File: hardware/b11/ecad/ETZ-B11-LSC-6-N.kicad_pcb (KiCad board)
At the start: 2 copper layers, 112.3 x 85.8 mm, 0 parts

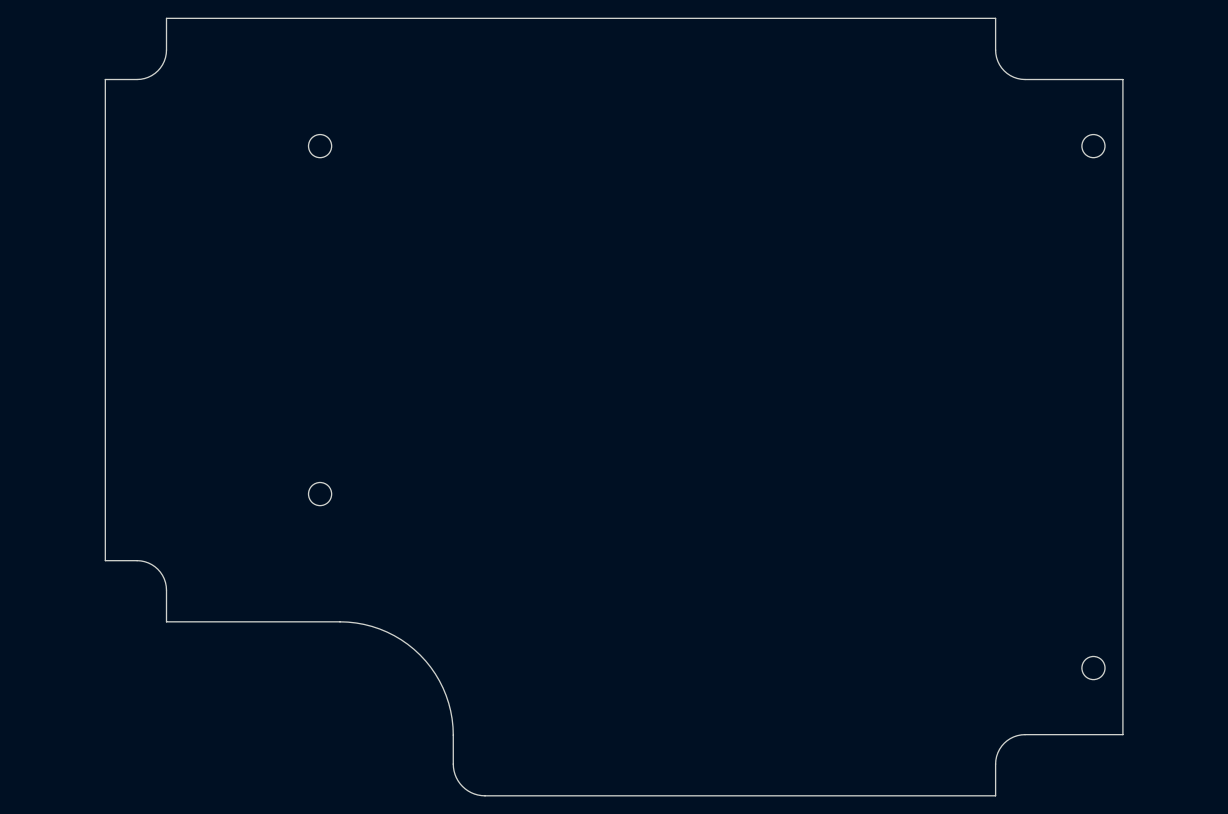
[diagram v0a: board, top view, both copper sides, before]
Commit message: feat(hardware/b11): place MX hotswap switches on normal-profile carrier PCBs
Add place-b11-switches.py with SWIG pre-init workaround (plug must be
created and FootprintLoad called before LoadBoard or SWIG type registry
gets corrupted). Layout: 5-col boards get 18 switches (15 main + 3
thumb at cols 2-4), 6-col get 22 (18 main + 4 thumb at cols 2-5).

Also refresh all 20 PCB outline DXFs from latest MCAD release and add
MX_V2 footprint library as a submodule.

Co-Authored-By: Claude Sonnet 4.6 <noreply@anthropic.com>
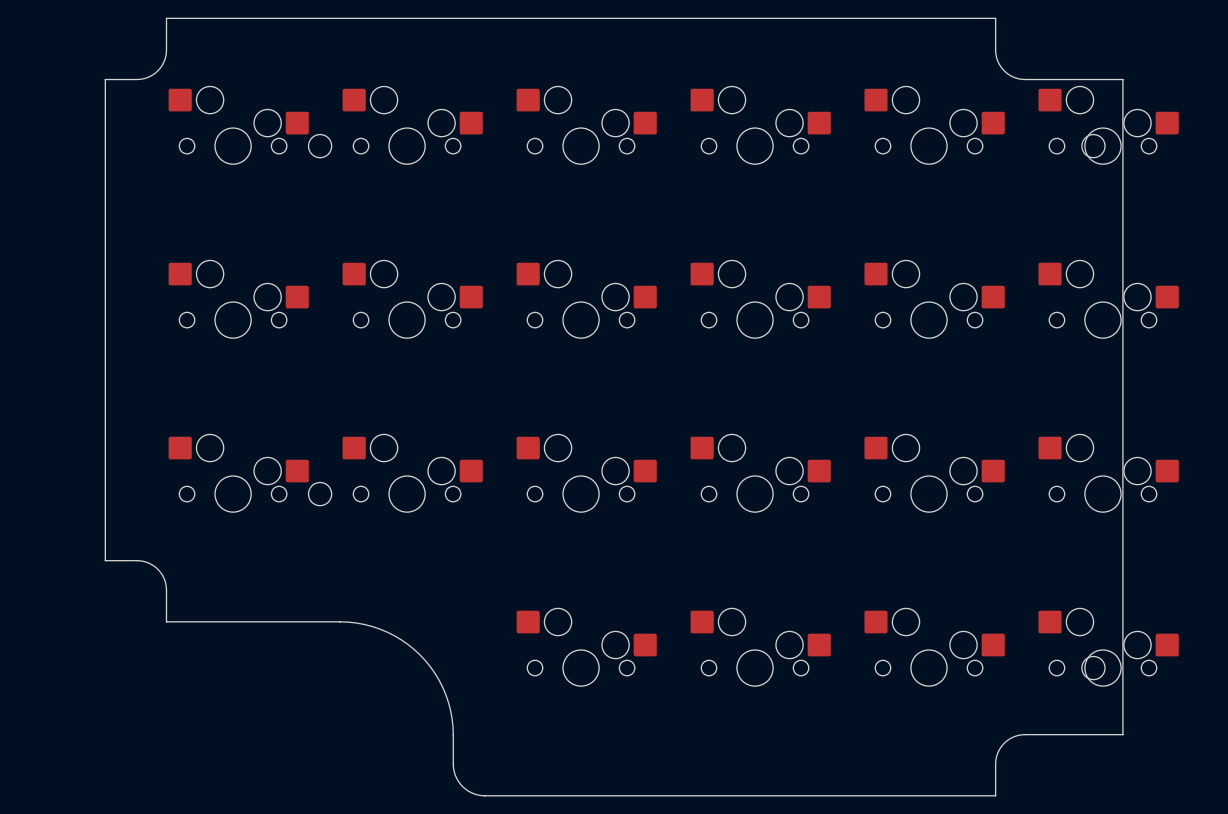
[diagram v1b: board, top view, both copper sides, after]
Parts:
- added SW1: MX-Hotswap-1U, MX-Hotswap-1U, F.Cu at (106.4, 73.3)
- added SW10: MX-Hotswap-1U, MX-Hotswap-1U, F.Cu at (164.0, 92.5)
- added SW11: MX-Hotswap-1U, MX-Hotswap-1U, F.Cu at (183.2, 92.5)
- added SW12: MX-Hotswap-1U, MX-Hotswap-1U, F.Cu at (202.4, 92.5)
- added SW13: MX-Hotswap-1U, MX-Hotswap-1U, F.Cu at (106.4, 111.7)
- added SW14: MX-Hotswap-1U, MX-Hotswap-1U, F.Cu at (125.6, 111.7)
- added SW15: MX-Hotswap-1U, MX-Hotswap-1U, F.Cu at (144.8, 111.7)
- added SW16: MX-Hotswap-1U, MX-Hotswap-1U, F.Cu at (164.0, 111.7)
- added SW17: MX-Hotswap-1U, MX-Hotswap-1U, F.Cu at (183.2, 111.7)
- added SW18: MX-Hotswap-1U, MX-Hotswap-1U, F.Cu at (202.4, 111.7)
- added SW19: MX-Hotswap-1U, MX-Hotswap-1U, F.Cu at (144.8, 130.9)
- added SW2: MX-Hotswap-1U, MX-Hotswap-1U, F.Cu at (125.6, 73.3)
- added SW20: MX-Hotswap-1U, MX-Hotswap-1U, F.Cu at (164.0, 130.9)
- added SW21: MX-Hotswap-1U, MX-Hotswap-1U, F.Cu at (183.2, 130.9)
- added SW22: MX-Hotswap-1U, MX-Hotswap-1U, F.Cu at (202.4, 130.9)
- added SW3: MX-Hotswap-1U, MX-Hotswap-1U, F.Cu at (144.8, 73.3)
- added SW4: MX-Hotswap-1U, MX-Hotswap-1U, F.Cu at (164.0, 73.3)
- added SW5: MX-Hotswap-1U, MX-Hotswap-1U, F.Cu at (183.2, 73.3)
- added SW6: MX-Hotswap-1U, MX-Hotswap-1U, F.Cu at (202.4, 73.3)
- added SW7: MX-Hotswap-1U, MX-Hotswap-1U, F.Cu at (106.4, 92.5)
- added SW8: MX-Hotswap-1U, MX-Hotswap-1U, F.Cu at (125.6, 92.5)
- added SW9: MX-Hotswap-1U, MX-Hotswap-1U, F.Cu at (144.8, 92.5)

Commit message: fix(hardware/b11): correct 6-col PCB outlines and regenerate all boards
Update DXF outlines for all 6-col variants (LSC, RSC, LSP, RSP — both
normal and low profile) exported manually from OnShape with the _6
configuration. Regenerate all 16 KiCad PCBs from the corrected outlines
and re-place MX hotswap switches on the 4 normal-profile carrier boards.

Co-Authored-By: Claude Sonnet 4.6 <noreply@anthropic.com>
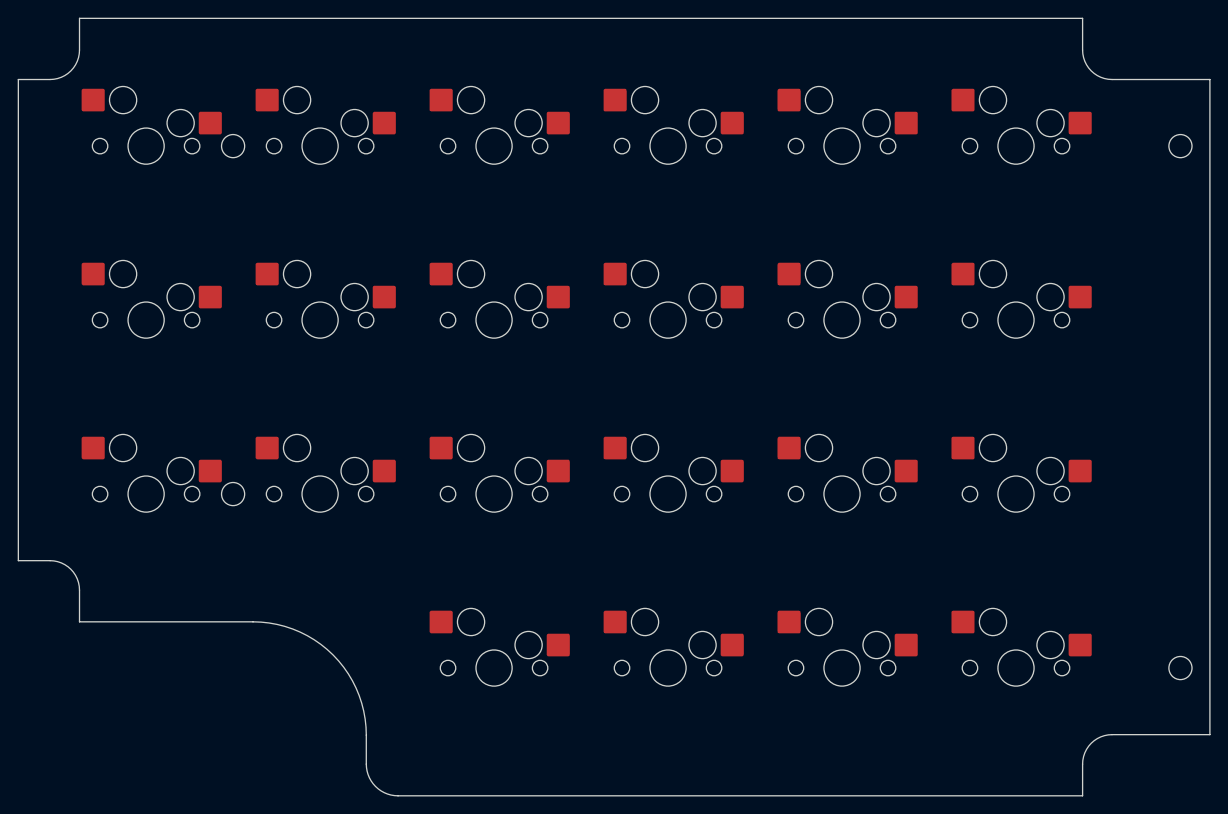
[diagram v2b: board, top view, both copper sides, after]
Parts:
- moved SW11 9.60 mm to (173.6, 92.5)
- moved SW17 9.60 mm to (173.6, 111.7)
- moved SW21 9.60 mm to (173.6, 130.9)
- moved SW5 9.60 mm to (173.6, 73.3)
- moved SW10 9.60 mm to (154.4, 92.5)
- moved SW16 9.60 mm to (154.4, 111.7)
- moved SW20 9.60 mm to (154.4, 130.9)
- moved SW4 9.60 mm to (154.4, 73.3)
- moved SW1 9.60 mm to (96.8, 73.3)
- moved SW13 9.60 mm to (96.8, 111.7)
- moved SW7 9.60 mm to (96.8, 92.5)
- moved SW12 9.60 mm to (192.8, 92.5)
- moved SW14 9.60 mm to (116.0, 111.7)
- moved SW15 9.60 mm to (135.2, 111.7)
- moved SW18 9.60 mm to (192.8, 111.7)
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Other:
- board size 112.3 x 85.8 mm -> 131.5 x 85.8 mm

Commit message: feat(hardware/b11): place hotswap sockets on all carrier boards, south-facing
- Place Kailh MX hotswap sockets (MX-Hotswap-1U) on 4 normal-profile carrier
  boards at 19.2mm pitch, flipped to B.Cu, 180° south-facing orientation
- Place Kailh Choc v1 hotswap sockets (PG1350) on 4 low-profile carrier boards
  at 19.2mm pitch, 180° south-facing orientation
- Add 3D model (Kailh-Choc-Socket-CPG135001S30.step) to PG1350 footprint with
  correct offset/rotation for B.Cu-pad, F.Cu-module placement
- Strip F.SilkS, F.Fab, F.CrtYd top-layer graphics from LP carrier PG1350 footprints
- Rename place-b11-switches.py → place-b11-switches-np.py for symmetry with new lp script
- Add place-b11-switches-lp.py for Choc v1 placement automation

Co-Authored-By: Claude Sonnet 4.6 <noreply@anthropic.com>
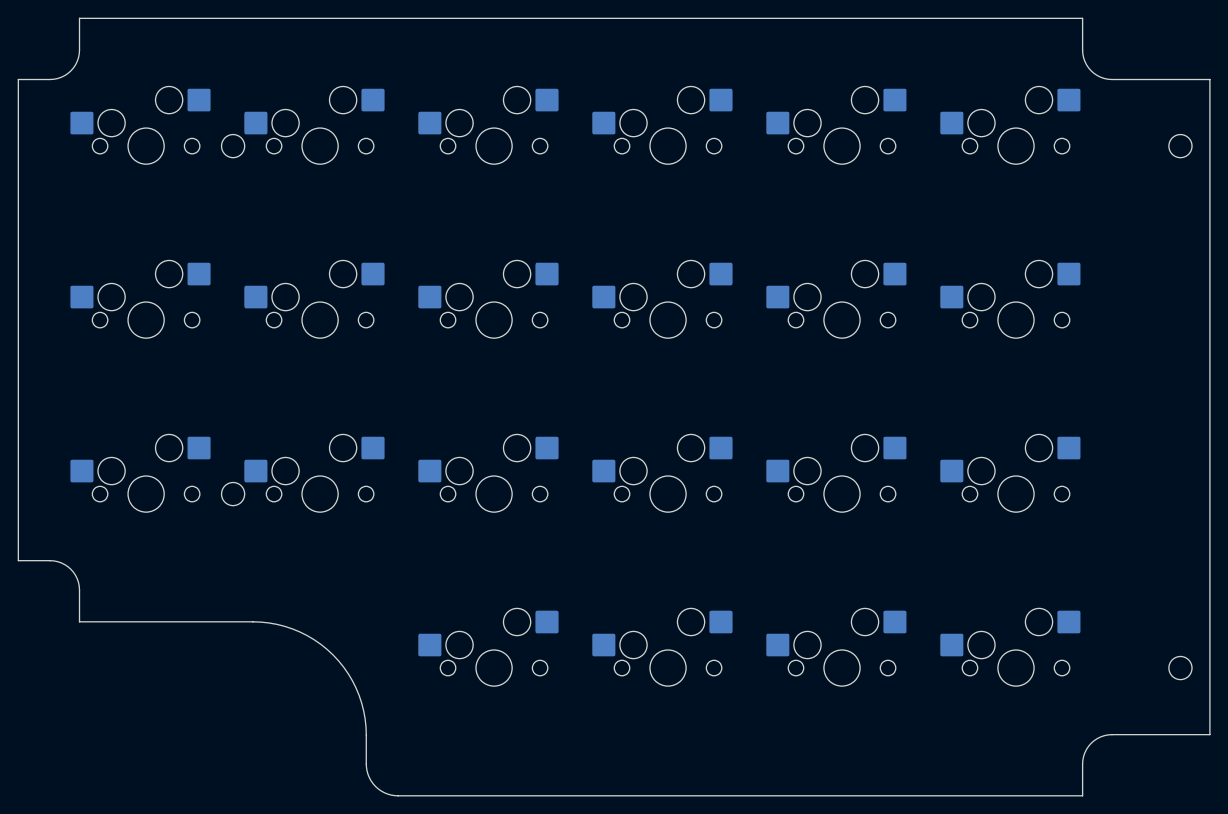
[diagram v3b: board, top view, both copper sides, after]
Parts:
- SW1, SW10, SW11, SW12, SW13, SW14, SW15, SW16, SW17, SW18, SW19, SW2, SW20, SW21, SW22, SW3, SW4, SW5, SW6, SW7, SW8, SW9: moved to B.Cu
- turned SW1 to 180 degrees
- turned SW10 to 180 degrees
- turned SW11 to 180 degrees
- turned SW12 to 180 degrees
- turned SW13 to 180 degrees
- turned SW14 to 180 degrees
- turned SW15 to 180 degrees
- turned SW16 to 180 degrees
- turned SW17 to 180 degrees
- turned SW18 to 180 degrees
- turned SW19 to 180 degrees
- turned SW2 to 180 degrees
- turned SW20 to 180 degrees
- turned SW21 to 180 degrees
- turned SW22 to 180 degrees
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
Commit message: feat(hardware/b11): add SMD 6028 back-mount LED footprint and place on all carrier PCBs
- Add LED_SMD_6028_BackMount footprint with router-safe rounded-rectangle
  slot cutout (3.3 × 3.9 mm, 0.5 mm corners, 1 mm bit), roundrect pads
  (1.4 × 2.8 mm, 25% ratio), silkscreen polarity markers clear of pads
- Add LED_SMD_6028.step 3D model from 3D Content Central
- Add place-b11-leds.py: places 18–22 LEDs per carrier PCB aligned to
  the switch grid, 5.9 mm south of each switch center
- Place LEDs on all 8 carrier PCBs (LSC/RSC × 5/6-col × N/L)

Co-Authored-By: Claude Sonnet 4.6 <noreply@anthropic.com>
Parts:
- added LED1: LED_SMD_6028_BackMount, LED_SMD_6028_BackMount, B.Cu at (96.8, 79.2)
- added LED10: LED_SMD_6028_BackMount, LED_SMD_6028_BackMount, B.Cu at (154.4, 98.4)
- added LED11: LED_SMD_6028_BackMount, LED_SMD_6028_BackMount, B.Cu at (173.6, 98.4)
- added LED12: LED_SMD_6028_BackMount, LED_SMD_6028_BackMount, B.Cu at (192.8, 98.4)
- added LED13: LED_SMD_6028_BackMount, LED_SMD_6028_BackMount, B.Cu at (96.8, 117.6)
- added LED14: LED_SMD_6028_BackMount, LED_SMD_6028_BackMount, B.Cu at (116.0, 117.6)
- added LED15: LED_SMD_6028_BackMount, LED_SMD_6028_BackMount, B.Cu at (135.2, 117.6)
- added LED16: LED_SMD_6028_BackMount, LED_SMD_6028_BackMount, B.Cu at (154.4, 117.6)
- added LED17: LED_SMD_6028_BackMount, LED_SMD_6028_BackMount, B.Cu at (173.6, 117.6)
- added LED18: LED_SMD_6028_BackMount, LED_SMD_6028_BackMount, B.Cu at (192.8, 117.6)
- added LED19: LED_SMD_6028_BackMount, LED_SMD_6028_BackMount, B.Cu at (135.2, 136.8)
- added LED2: LED_SMD_6028_BackMount, LED_SMD_6028_BackMount, B.Cu at (116.0, 79.2)
- added LED20: LED_SMD_6028_BackMount, LED_SMD_6028_BackMount, B.Cu at (154.4, 136.8)
- added LED21: LED_SMD_6028_BackMount, LED_SMD_6028_BackMount, B.Cu at (173.6, 136.8)
- added LED22: LED_SMD_6028_BackMount, LED_SMD_6028_BackMount, B.Cu at (192.8, 136.8)
- added LED3: LED_SMD_6028_BackMount, LED_SMD_6028_BackMount, B.Cu at (135.2, 79.2)
- added LED4: LED_SMD_6028_BackMount, LED_SMD_6028_BackMount, B.Cu at (154.4, 79.2)
- added LED5: LED_SMD_6028_BackMount, LED_SMD_6028_BackMount, B.Cu at (173.6, 79.2)
- added LED6: LED_SMD_6028_BackMount, LED_SMD_6028_BackMount, B.Cu at (192.8, 79.2)
- added LED7: LED_SMD_6028_BackMount, LED_SMD_6028_BackMount, B.Cu at (96.8, 98.4)
- added LED8: LED_SMD_6028_BackMount, LED_SMD_6028_BackMount, B.Cu at (116.0, 98.4)
- added LED9: LED_SMD_6028_BackMount, LED_SMD_6028_BackMount, B.Cu at (135.2, 98.4)

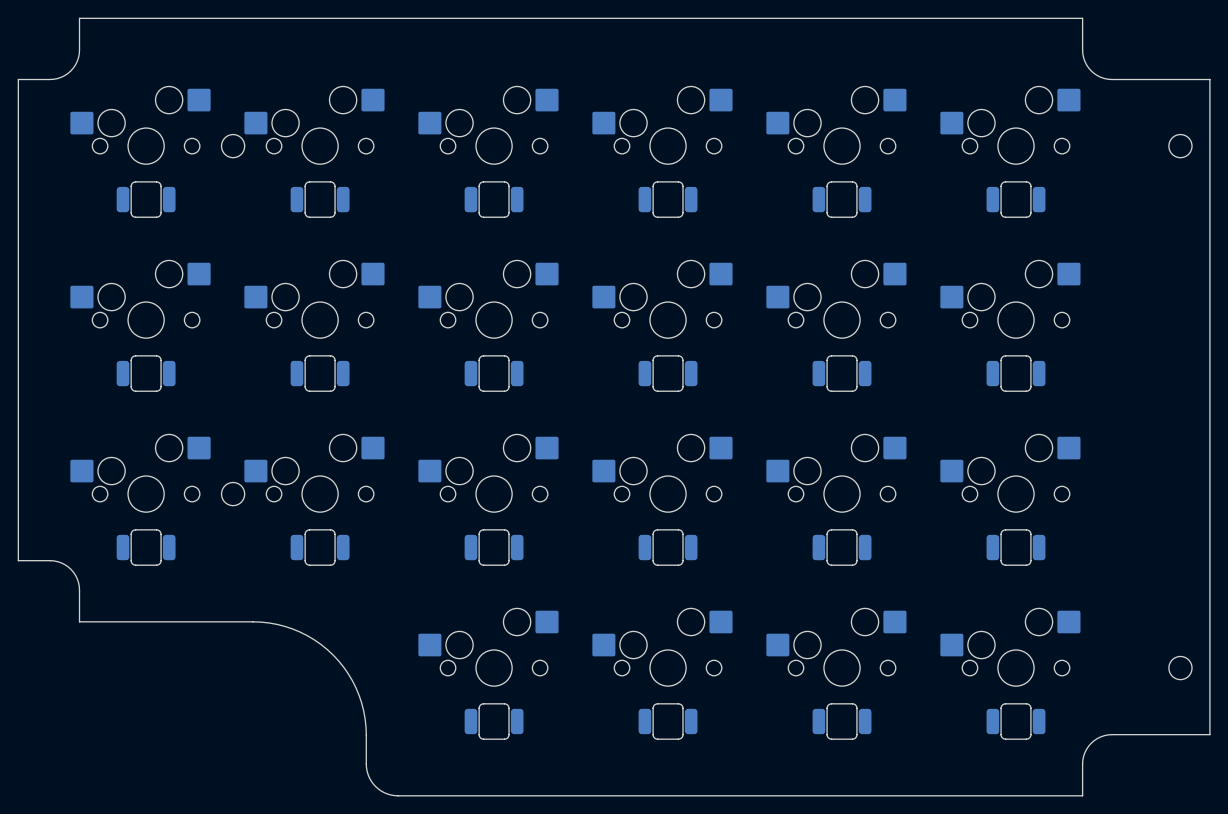
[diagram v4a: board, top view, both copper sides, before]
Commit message: fix(hardware/b11): fix switch socket placement, 3D models, and submodule pins
- Pin MX_V2 submodule to ab59b57 (before upstream "topside pads" change that
  moved SMD pads to F.Cu — old commit has correct B.Cu pads natively)
- Fix SWIG type-registry corruption in both switch placement scripts by
  pre-loading all footprint instances and caching pad refs before LoadBoard()
- Fix LP script: add make_patched_lib to rewrite Choc socket 3D model path
  to absolute path and convert old (at ...) inch offset to (offset ...) mm
  format — KiCad 9 was multiplying the old format by 25.4, placing model
  127mm off-center
- Regenerate all 8 carrier PCBs with updated board outlines (LSC-6 mounting
  hole positions) and correctly placed switches + LEDs

Co-Authored-By: Claude Sonnet 4.6 <noreply@anthropic.com>
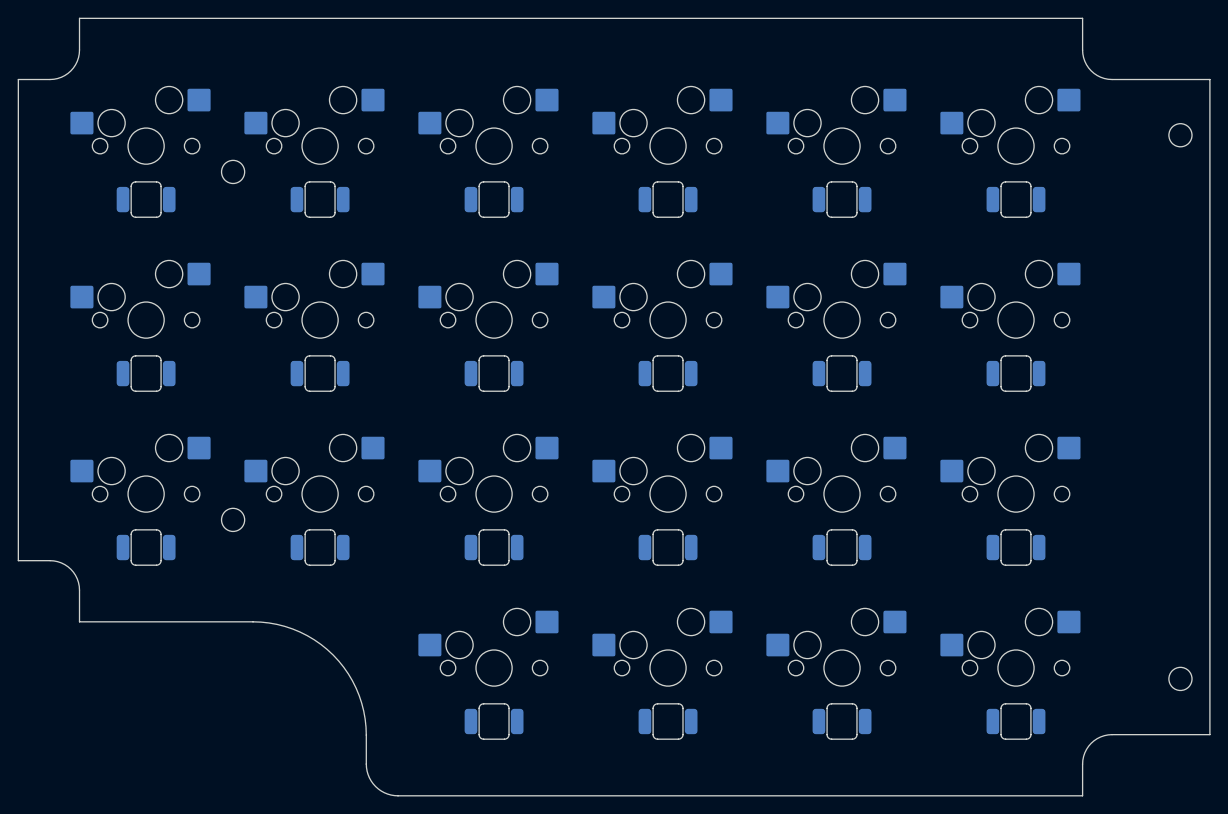
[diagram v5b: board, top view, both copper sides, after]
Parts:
- SW1, SW10, SW11, SW12, SW13, SW14, SW15, SW16, SW17, SW18, SW19, SW2, SW20, SW21, SW22, SW3, SW4, SW5, SW6, SW7, SW8, SW9: moved to F.Cu
- turned SW1 to 0 degrees
- turned SW10 to 0 degrees
- turned SW11 to 0 degrees
- turned SW12 to 0 degrees
- turned SW13 to 0 degrees
- turned SW14 to 0 degrees
- turned SW15 to 0 degrees
- turned SW16 to 0 degrees
- turned SW17 to 0 degrees
- turned SW18 to 0 degrees
- turned SW19 to 0 degrees
- turned SW2 to 0 degrees
- turned SW20 to 0 degrees
- turned SW21 to 0 degrees
- turned SW22 to 0 degrees
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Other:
- outline, holes or cut-outs redrawn
